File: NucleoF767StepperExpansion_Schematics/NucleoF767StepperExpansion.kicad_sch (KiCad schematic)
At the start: 1 part, among them Q1 SSM3K339R,LF

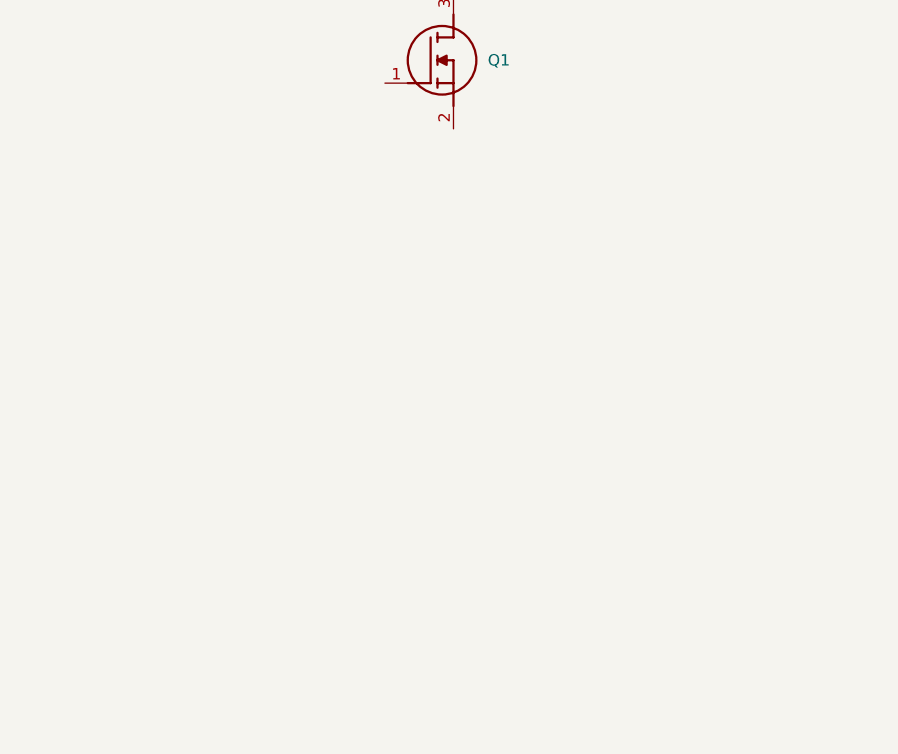
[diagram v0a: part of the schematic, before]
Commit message: Add terminal blocks and connector components~
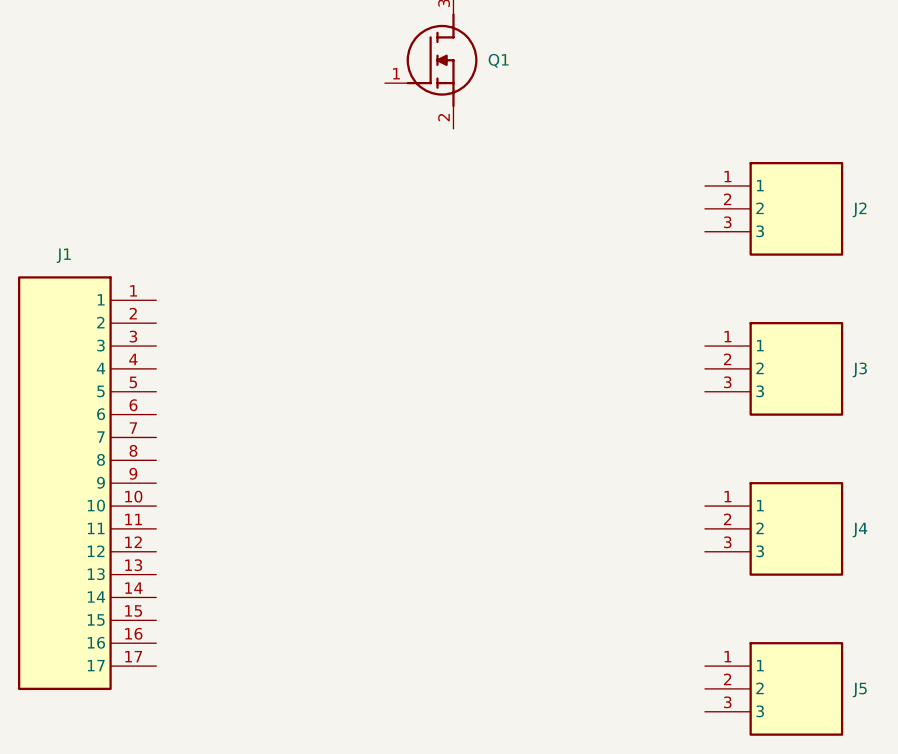
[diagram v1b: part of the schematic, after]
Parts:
- added J1: TSW-117-07-L-S, TSW-117-XX-YY-S, symbol NucleoF767StepperExpansion_Symbols:TSW-117-07-L-S
- added J2, J3, J4, J5: 1715734, 1715734, symbol NucleoF767StepperExpansion_Symbols:1715734

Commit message: Updated schematics
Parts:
- added J6: 1715734, 1715734, symbol NucleoF767StepperExpansion_Symbols:1715734
- added Q10, Q11, Q12, Q2, Q3, Q4, Q5, Q6, Q7, Q8, Q9: SSM3K339R,LF, NucleoF767StepperExpansion_Footprints:SOTFL95P240X88-3N, symbol NucleoF767StepperExpansion_Symbols:SSM3K339R,LF
- added R1, R11, R13, R15, R17, R19, R21, R23, R3, R5, R7, R9: 100R, Resistor_SMD:R_0603_1608Metric_Pad0.98x0.95mm_HandSolder, symbol Device:R_Small
- added R10, R12, R14, R16, R18, R2, R20, R22, R24, R4, R6, R8: 10k, Resistor_SMD:R_0603_1608Metric_Pad0.98x0.95mm_HandSolder, symbol Device:R_Small
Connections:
- net at J3.1: now also Q4.3 (D)
- net at J3.2: now also Q5.3 (D)
- net at J3.3: now also Q6.3 (D)
- net M1_pul: now reaches J1.1
- net M1_pul: now also R1.1
- net M3_dir: now reaches J1.10
- net M3_dir: now also R15.1
- net GND: now reaches J1.11
- net GND: now also Q1.2 (S), J6.1, J6.2, J6.3, Q10.2 (S), Q11.2 (S), Q12.2 (S), Q2.2 (S), Q3.2 (S), Q4.2 (S), Q5.2 (S), Q6.2 (S), Q7.2 (S), Q8.2 (S), Q9.2 (S), R10.1, R12.1, R14.1, R16.1, R18.1, R2.1, R20.1, R22.1, R24.1, R4.1, R6.1, R8.1
- net M3_ena: now reaches J1.12
- net M3_ena: now also R17.1
- net M2_break: now reaches J1.13
- net M2_break: now also R19.1
- net Spare1: now reaches J1.14
- net Spare1: now also R21.1
- net Spare2: now reaches J1.15
- net Spare2: now also R23.1
- net M1_dir: now reaches J1.2
- net M1_dir: now also R3.1
- net M1_ena: now reaches J1.3
- net M1_ena: now also R5.1
- net M2_pul: now reaches J1.4
- net M2_pul: now also R7.1
- net M2_dir: now reaches J1.5
- net M2_dir: now also R9.1
- net M2_ena: now reaches J1.6
- net M2_ena: now also R11.1
- net M3_pul: now reaches J1.9
- net M3_pul: now also R13.1
- net at J2.1: now also Q1.3 (D)
- net at J2.2: now also Q2.3 (D)
- net at J2.3: now also Q3.3 (D)
- net at J4.1: now also Q7.3 (D)
- net at J4.2: now also Q8.3 (D)
- net at J4.3: now also Q9.3 (D)
- net at J5.1: now also Q10.3 (D)
- net at J5.2: now also Q11.3 (D)
- net at J5.3: now also Q12.3 (D)
- net at Q1.1 (G): now also R1.2, R2.2
- new net: Q3.1 (G), R5.2, R6.2
- new net: Q4.1 (G), R7.2, R8.2
- new net: Q12.1 (G), R23.2, R24.2
- new net: Q7.1 (G), R13.2, R14.2
- new net: Q10.1 (G), R19.2, R20.2
- new net: Q2.1 (G), R3.2, R4.2
- new net: Q8.1 (G), R15.2, R16.2
- new net: Q9.1 (G), R17.2, R18.2
- new net: Q5.1 (G), R10.2, R9.2
- new net: Q6.1 (G), R11.2, R12.2
- new net: Q11.1 (G), R21.2, R22.2
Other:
- note added: "Spare"
- note added: "Stepper 1 control"
- note added: "Stepper 2 control"
- note added: "Stepper 3 control"
- moved on the sheet: J1, J2, Q1

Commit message: Updated schematics and PCB
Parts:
- J1: footprint TSW-117-XX-YY-S -> NucleoF767StepperExpansion_Footprints:TSW-117-XX-YY-S
- J2, J3, J4, J5, J6: footprint 1715734 -> NucleoF767StepperExpansion_Footprints:1715734
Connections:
- no-connect marks 0 -> 4
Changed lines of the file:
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@@
 		(color 0 0 0 0)
 	)
+	(no_connect
+		(at 259.08 86.36)
+	)
+	(no_connect
+		(at 259.08 106.68)
+	)
+	(no_connect
+		(at 259.08 109.22)
+	)
+	(no_connect
+		(at 259.08 83.82)
+	)
 	(wire
 		(pts
@@
 			)
 		)
-		(property "Footprint" "1715734"
+		(property "Footprint" "NucleoF767StepperExpansion_Footprints:1715734"
 			(at 95.25 96.52 0)
 			(hide yes)
@@
 	(symbol
 		(lib_id "power:GND")
+		(at 33.02 34.29 0)
+		(unit 1)
+		(body_style 1)
+		(exclude_from_sim no)
+		(in_bom yes)
+		(on_board yes)
+		(in_pos_files yes)
+		(dnp no)
+		(fields_autoplaced yes)
+		(property "Reference" "#PWR027"
+			(at 33.02 40.64 0)
+			(hide yes)
+			(show_name no)
+			(do_not_autoplace no)
+			(effects
+				(font
+					(size 1.27 1.27)
+				)
+			)
+		)
+		(property "Value" "GND"
+			(at 33.02 39.37 0)
+			(show_name no)
+			(do_not_autoplace no)
+			(effects
+				(font
+					(size 1.27 1.27)
+				)
+			)
+		)
+		(property "Footprint" ""
+			(at 33.02 34.29 0)
+			(hide yes)
+			(show_name no)
+			(do_not_autoplace no)
+			(effects
+				(font
+					(size 1.27 1.27)
+				)
+			)
+		)
+		(property "Datasheet" ""
+			(at 33.02 34.29 0)
+			(hide yes)
+			(show_name no)
+			(do_not_autoplace no)
+			(effects
+				(font
+					(size 1.27 1.27)
+				)
+			)
+		)
+		(property "Description" "Power symbol creates a global label with name \"GND\" , ground"
+			(at 33.02 34.29 0)
+			(hide yes)
+			(show_name no)
+			(do_not_autoplace no)
+			(effects
+				(font
+					(size 1.27 1.27)
+				)
+			)
+		)
+		(pin "1"
+		)
+		(instances
+			(project "NucleoF767StepperExpansion"
+				(path "/bc8f7c8e-bae0-472c-af5a-f214b9a78cc2"
+					(reference "#PWR027")
+					(unit 1)
+				)
+			)
+		)
+	)
+	(symbol
+		(lib_id "power:GND")
 		(at 39.37 165.1 0)
 		(unit 1)
@@
 			)
 		)
-		(property "Footprint" "1715734"
+		(property "Footprint" "NucleoF767StepperExpansion_Footprints:1715734"
 			(at 207.01 96.52 0)
 			(hide yes)
@@
 			)
 		)
-		(property "Footprint" "TSW-117-XX-YY-S"
+		(property "Footprint" "NucleoF767StepperExpansion_Footprints:TSW-117-XX-YY-S"
 			(at 246.634 116.586 0)
 			(hide yes)
@@
 			)
 		)
-		(property "Footprint" "1715734"
+		(property "Footprint" "NucleoF767StepperExpansion_Footprints:1715734"
 			(at 95.25 33.02 0)
 			(hide yes)
@@
 	)
 	(symbol
+		(lib_id "power:PWR_FLAG")
+		(at 33.02 34.29 0)
+		(unit 1)
+		(body_style 1)
+		(exclude_from_sim no)
+		(in_bom yes)
+		(on_board yes)
+		(in_pos_files yes)
+		(dnp no)
+		(fields_autoplaced yes)
+		(property "Reference" "#FLG01"
+			(at 33.02 32.385 0)
+			(hide yes)
+			(show_name no)
+			(do_not_autoplace no)
+			(effects
+				(font
+					(size 1.27 1.27)
+				)
+			)
+		)
+		(property "Value" "PWR_FLAG"
+			(at 33.02 29.21 0)
+			(show_name no)
+			(do_not_autoplace no)
+			(effects
+				(font
+					(size 1.27 1.27)
+				)
+			)
+		)
+		(property "Footprint" ""
+			(at 33.02 34.29 0)
+			(hide yes)
+			(show_name no)
+			(do_not_autoplace no)
+			(effects
+				(font
+					(size 1.27 1.27)
+				)
+			)
+		)
+		(property "Datasheet" ""
+			(at 33.02 34.29 0)
+			(hide yes)
+			(show_name no)
+			(do_not_autoplace no)
+			(effects
+				(font
+					(size 1.27 1.27)
+				)
+			)
+		)
+		(property "Description" "Special symbol for telling ERC where power comes from"
+			(at 33.02 34.29 0)
+			(hide yes)
+			(show_name no)
+			(do_not_autoplace no)
+			(effects
+				(font
+					(size 1.27 1.27)
+				)
+			)
+		)
+		(pin "1"
+		)
+		(instances
+			(project "NucleoF767StepperExpansion"
+				(path "/bc8f7c8e-bae0-472c-af5a-f214b9a78cc2"
+					(reference "#FLG01")
+					(unit 1)
+				)
+			)
+		)
+	)
+	(symbol
 		(lib_id "power:GND")
 		(at 215.9 128.27 0)
@@
 			)
 		)
-		(property "Footprint" "1715734"
+		(property "Footprint" "NucleoF767StepperExpansion_Footprints:1715734"
 			(at 57.15 158.75 0)
 			(hide yes)
@@
 			)
 		)
-		(property "Footprint" "1715734"
+		(property "Footprint" "NucleoF767StepperExpansion_Footprints:1715734"
 			(at 207.01 33.02 0)
 			(hide yes)
